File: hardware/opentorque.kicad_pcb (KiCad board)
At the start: 2 copper layers, 27 parts, among them SW1 TS-1088-AR02016, U1 RP2040, U2 W25Q128JVSIQTR, X1 X322512MSB4SI

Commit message: Arrange components
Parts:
- added C16: 100n, Capacitor_SMD:C_0603_1608Metric, F.Cu at (164.0, 103.0)
- added C17: 100n, Capacitor_SMD:C_0603_1608Metric, F.Cu at (162.5, 92.2)
- added C18: 100n, Capacitor_SMD:C_0603_1608Metric, F.Cu at (166.5, 89.0)
- added C19: RVT1J221M1010, easyeda2kicad:CAP-SMD_BD10.0-L10.3-W10.3-FD, F.Cu at (155.5, 96.0)
- added C20: 100n, Capacitor_SMD:C_0603_1608Metric, F.Cu at (184.0, 103.0)
- added C21: 100n, Capacitor_SMD:C_0603_1608Metric, F.Cu at (182.5, 92.2)
- added C22: 100n, Capacitor_SMD:C_0603_1608Metric, F.Cu at (186.5, 89.0)
- added C23: RVT1J221M1010, easyeda2kicad:CAP-SMD_BD10.0-L10.3-W10.3-FD, F.Cu at (175.5, 96.0)
- added C24: 100n, Capacitor_SMD:C_0603_1608Metric, F.Cu at (204.0, 103.0)
- added C25: 100n, Capacitor_SMD:C_0603_1608Metric, F.Cu at (202.5, 92.2)
- added C26: 100n, Capacitor_SMD:C_0603_1608Metric, F.Cu at (206.5, 89.0)
- added C27: RVT1J221M1010, easyeda2kicad:CAP-SMD_BD10.0-L10.3-W10.3-FD, F.Cu at (195.5, 96.0)
- added D1: SS14_C2837270, easyeda2kicad:SMA_L4.3-W2.6-LS5.0-RD, F.Cu at (168.5, 98.0)
- added D2: SS14_C2837270, easyeda2kicad:SMA_L4.3-W2.6-LS5.0-RD, F.Cu at (188.5, 98.0)
- added D3: SS14_C2837270, easyeda2kicad:SMA_L4.3-W2.6-LS5.0-RD, F.Cu at (208.5, 98.0)
- added GND1: TestPoint, TestPoint:TestPoint_Pad_4.0x4.0mm, F.Cu at (190.0, 72.5)
- added Q1: 30N06_C5807887, easyeda2kicad:TO-252-2_L6.6-W6.1-P4.57-LS9.9-BR-CW, F.Cu at (153.5, 82.0)
- added Q2: 30N06_C5807887, easyeda2kicad:TO-252-2_L6.6-W6.1-P4.57-LS9.9-BR-CW, F.Cu at (160.5, 84.0)
- added Q3: 30N06_C5807887, easyeda2kicad:TO-252-2_L6.6-W6.1-P4.57-LS9.9-BR-CW, F.Cu at (173.5, 82.0)
- added Q4: 30N06_C5807887, easyeda2kicad:TO-252-2_L6.6-W6.1-P4.57-LS9.9-BR-CW, F.Cu at (180.5, 84.0)
- added Q5: 30N06_C5807887, easyeda2kicad:TO-252-2_L6.6-W6.1-P4.57-LS9.9-BR-CW, F.Cu at (193.5, 82.0)
- added Q6: 30N06_C5807887, easyeda2kicad:TO-252-2_L6.6-W6.1-P4.57-LS9.9-BR-CW, F.Cu at (200.5, 84.0)
- added R10: 1m, Resistor_SMD:R_1206_3216Metric, F.Cu at (165.5, 81.5)
- added R11: 27R, Resistor_SMD:R_0603_1608Metric, F.Cu at (184.0, 92.2)
- added R12: 27R, Resistor_SMD:R_0603_1608Metric, F.Cu at (185.5, 92.2)
- added R13: 1m, Resistor_SMD:R_1206_3216Metric, F.Cu at (185.5, 81.5)
- added R14: 27R, Resistor_SMD:R_0603_1608Metric, F.Cu at (204.0, 92.2)
- added R15: 27R, Resistor_SMD:R_0603_1608Metric, F.Cu at (205.5, 92.2)
- added R16: 1m, Resistor_SMD:R_1206_3216Metric, F.Cu at (205.5, 81.5)
- added R17: 20k, Resistor_SMD:R_0603_1608Metric, F.Cu at (166.7, 124.5)
- added R18: 1k, Resistor_SMD:R_0603_1608Metric, F.Cu at (166.7, 126.0)
- added R8: 27R, Resistor_SMD:R_0603_1608Metric, F.Cu at (164.0, 92.2)
- added R9: 27R, Resistor_SMD:R_0603_1608Metric, F.Cu at (165.5, 92.2)
- added REF**: MountingHole_3.2mm_M3, MountingHole:MountingHole_3.2mm_M3, F.Cu at (153.5, 73.5)
- added REF**: MountingHole_3.2mm_M3, MountingHole:MountingHole_3.2mm_M3, F.Cu at (153.5, 126.5)
- added REF**: MountingHole_3.2mm_M3, MountingHole:MountingHole_3.2mm_M3, F.Cu at (206.5, 126.5)
- added REF**: MountingHole_3.2mm_M3, MountingHole:MountingHole_3.2mm_M3, F.Cu at (206.5, 73.5)
- added TP1: TestPoint, TestPoint:TestPoint_Pad_4.0x4.0mm, F.Cu at (160.0, 72.5)
- added TP2: TestPoint, TestPoint:TestPoint_Pad_4.0x4.0mm, F.Cu at (180.0, 72.5)
- added TP3: TestPoint, TestPoint:TestPoint_Pad_4.0x4.0mm, F.Cu at (200.0, 72.5)
- added U10: AMS1117-5.0_C347223, easyeda2kicad:SOT-223_L6.7-W3.5-P2.30-BR, F.Cu at (168.4, 109.7)
- added U11: AMS1117-3.3_C347222, easyeda2kicad:SOT-223-4_L6.5-W3.5-P2.30-LS7.0-BR, F.Cu at (168.7, 117.2)
- added U3: SLM2003ECA-DG, easyeda2kicad:SOIC-8_L4.9-W3.9-P1.27-LS6.0-BL, F.Cu at (164.0, 98.0)
- added U4: INA180A3IDBVR, easyeda2kicad:SOT-23-5_L3.0-W1.7-P0.95-LS2.8-BR, F.Cu at (166.5, 86.0)
- added U5: SLM2003ECA-DG, easyeda2kicad:SOIC-8_L4.9-W3.9-P1.27-LS6.0-BL, F.Cu at (184.0, 98.0)
- added U6: INA180A3IDBVR, easyeda2kicad:SOT-23-5_L3.0-W1.7-P0.95-LS2.8-BR, F.Cu at (186.5, 86.0)
- added U7: SLM2003ECA-DG, easyeda2kicad:SOIC-8_L4.9-W3.9-P1.27-LS6.0-BL, F.Cu at (204.0, 98.0)
- added U8: INA180A3IDBVR, easyeda2kicad:SOT-23-5_L3.0-W1.7-P0.95-LS2.8-BR, F.Cu at (206.5, 86.0)
- added U9: UMW78M12, easyeda2kicad:TO-252-2_L6.6-W6.1-P4.57-LS9.9-BR-CW, F.Cu at (158.0, 110.5)
- added VCC_12-56: TestPoint, TestPoint:TestPoint_Pad_4.0x4.0mm, F.Cu at (170.0, 72.5)
- moved R4 93.0 mm to (194.5, 124.0), turned to 90 degrees
- moved C11 91.8 mm to (200.8, 117.0)
- moved C12 91.8 mm to (200.8, 119.5)
- moved C3 91.8 mm to (196.8, 112.0)
- moved C5 91.8 mm to (196.8, 117.0)
- moved C6 91.8 mm to (196.8, 119.5)
- moved C8 91.8 mm to (200.8, 109.5)
- moved C9 91.8 mm to (200.8, 112.0)
- moved C10 91.8 mm to (200.8, 114.5)
- moved C13 91.8 mm to (204.8, 107.0)
- moved C14 91.8 mm to (204.8, 109.5)
- moved C15 91.8 mm to (204.8, 112.0)
- moved C4 91.8 mm to (196.8, 114.5)
- moved C7 91.8 mm to (200.8, 107.0)
- moved R5 89.6 mm to (196.0, 124.0), turned to 90 degrees
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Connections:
- net +1V1 renamed /rp2040/1.1V
- net +3.3V renamed /rp2040/3.3V
- net +5V renamed /rp2040/5V
- net GND renamed /rp2040/GND
- U1 pad 2: /rp2040/GPIO0 -> /phasedriver U/HIN
- U1 pad 3: /rp2040/GPIO1 -> /phasedriver U/LINN
- U1 pad 38: /rp2040/GPIO26 -> /phasedriver U/AOUT
- U1 pad 39: /rp2040/GPIO27 -> /phasedriver V/AOUT
- U1 pad 4: /rp2040/GPIO2 -> /phasedriver V/HIN
- U1 pad 40: /rp2040/GPIO28 -> /phasedriver W/AOUT
- U1 pad 41: /rp2040/GPIO29 -> /<NO NET>
- U1 pad 5: /rp2040/GPIO3 -> /phasedriver V/LINN
- U1 pad 6: /rp2040/GPIO4 -> /phasedriver W/HIN
- U1 pad 7: /rp2040/GPIO5 -> /phasedriver W/LINN
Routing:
- net /rp2040/GND: track 15.1 -> 0.00 mm
- net /rp2040/5V: track 6.66 -> 0.00 mm
- net /rp2040/DP: track 5.32 -> 0.00 mm
- net Net-(USB1-DN1): track 4.73 -> 0.00 mm
- net /rp2040/DN: track 4.70 -> 0.00 mm
- net Net-(USB1-DP1): track 4.54 -> 0.00 mm
- net Net-(USB1-CC1): track 4.32 -> 0.00 mm
- net Net-(USB1-CC2): track 3.85 -> 0.00 mm
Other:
- board outline added: 60 x 60 mm

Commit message: Add more routing
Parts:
- removed C5: 100n, Capacitor_SMD:C_0603_1608Metric
- removed R6, R7: 5k1, Resistor_SMD:R_0603_1608Metric
- removed REF** (x4): MountingHole_3.2mm_M3, MountingHole:MountingHole_3.2mm_M3
- added C28: 100n, Capacitor_SMD:C_0603_1608Metric, B.Cu at (175.8, 97.5)
- U10: value AMS1117-5.0_C347223 -> AS5600-ASOT; footprint easyeda2kicad:SOT-223_L6.7-W3.5-P2.30-BR -> easyeda2kicad:SOIC-8_L5.0-W4.0-P1.27-LS6.0-BL; moved to B.Cu
- moved C10 28.4 mm to (172.5, 117.0), turned to 180 degrees
- moved C13 26.3 mm to (178.5, 106.0), turned to 90 degrees
- moved C11 25.9 mm to (175.0, 119.5), turned to -90 degrees
- moved C6 25.8 mm to (172.5, 111.0), turned to 180 degrees
- moved C3 24.6 mm to (172.5, 115.5), turned to 180 degrees
- moved C14 24.5 mm to (182.5, 119.5), turned to -90 degrees
- moved C12 24.3 mm to (176.5, 119.5), turned to -90 degrees
- moved C9 21.2 mm to (181.0, 119.5), turned to -90 degrees
- moved C4 18.8 mm to (180.0, 106.0), turned to 90 degrees
- moved D1 16.5 mm to (152.0, 97.5)
- moved D2 16.5 mm to (172.0, 97.5)
- moved D3 16.5 mm to (192.0, 97.5)
- moved C7 15.8 mm to (186.2, 113.0)
- moved C15 15.3 mm to (196.0, 124.5), turned to 90 degrees
- moved U10 15.1 mm to (180.0, 100.0)
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- renumbered GND1 to GND, TP1 to U, TP2 to V, TP3 to W
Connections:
- C1 pad 1: /rp2040/GND -> GND
- C10 pad 1: /rp2040/3.3V -> +3V3
- C10 pad 2: /rp2040/GND -> GND
- C11 pad 1: /rp2040/3.3V -> +3V3
- C11 pad 2: /rp2040/GND -> GND
- C12 pad 2: /rp2040/GND -> GND
- C13 pad 2: /rp2040/GND -> GND
- C14 pad 2: /rp2040/GND -> GND
- C15 pad 2: /rp2040/GND -> GND
- C18 pad 1: +5V -> +3V3
- C2 pad 1: /rp2040/GND -> GND
- C22 pad 1: +5V -> +3V3
- C26 pad 1: +5V -> +3V3
- C3 pad 1: /rp2040/3.3V -> +3V3
- C3 pad 2: /rp2040/GND -> GND
- C4 pad 1: /rp2040/3.3V -> +3V3
- C4 pad 2: /rp2040/GND -> GND
- C6 pad 1: /rp2040/3.3V -> +3V3
- C6 pad 2: /rp2040/GND -> GND
- C7 pad 1: /rp2040/3.3V -> +3V3
- C7 pad 2: /rp2040/GND -> GND
- C8 pad 1: /rp2040/3.3V -> +3V3
- C8 pad 2: /rp2040/GND -> GND
- C9 pad 1: /rp2040/3.3V -> +3V3
- C9 pad 2: /rp2040/GND -> GND
- R5 pad 1: /rp2040/3.3V -> +3V3
- SW1 pad 1: /rp2040/GND -> GND
- U1 pad 1: /rp2040/3.3V -> +3V3
- U1 pad 10: /rp2040/3.3V -> +3V3
- U1 pad 13: /rp2040/GPIO10 -> /phasedriver W/HIN
- U1 pad 14: /rp2040/GPIO11 -> /phasedriver W/LINN
- U1 pad 19: /rp2040/GND -> GND
- U1 pad 2: /phasedriver U/HIN -> /rp2040/GPIO0
- U1 pad 22: /rp2040/3.3V -> +3V3
- U1 pad 26: /rp2040/3.3V -> +3V3
- U1 pad 29: /rp2040/GPIO18 -> /phasedriver V/HIN
- U1 pad 3: /phasedriver U/LINN -> /rp2040/GPIO1
- U1 pad 30: /rp2040/GPIO19 -> /phasedriver V/LINN
- U1 pad 31: /rp2040/GPIO20 -> /phasedriver U/HIN
- U1 pad 32: /rp2040/GPIO21 -> /phasedriver U/LINN
- U1 pad 33: /rp2040/3.3V -> +3V3
- U1 pad 4: /phasedriver V/HIN -> /rp2040/GPIO2
- U1 pad 42: /rp2040/3.3V -> +3V3
- U1 pad 43: /rp2040/3.3V -> +3V3
- U1 pad 44: /rp2040/3.3V -> +3V3
- U1 pad 48: /rp2040/3.3V -> +3V3
- U1 pad 49: /rp2040/3.3V -> +3V3
- U1 pad 5: /phasedriver V/LINN -> /rp2040/GPIO3
- U1 pad 57: /rp2040/GND -> GND
- U1 pad 6: /phasedriver W/HIN -> /rp2040/GPIO4
- U1 pad 7: /phasedriver W/LINN -> /rp2040/GPIO5
- U10 pad 1: GND -> +3V3
- U10 pad 2: +5V -> +3V3
- U10 pad 3: +12V -> unconnected-(U10-OUT-Pad3)
- U10 pad 4: +5V -> GND
- U11 pad 2: +3.3V -> +3V3
- U11 pad 3: +5V -> +12V
- U11 pad 4: +3.3V -> +3V3
- U2 pad 4: /rp2040/GND -> GND
- U4 pad 5: +5V -> +3V3
- U6 pad 5: +5V -> +3V3
- U8 pad 5: +5V -> +3V3
- USB1 pad 1: /rp2040/GND -> GND
- USB1 pad 10: Net-(USB1-CC2) -> unconnected-(USB1-CC2-Pad10)
- USB1 pad 11: /rp2040/5V -> unconnected-(USB1-VBUS-Pad11)
- USB1 pad 12: /rp2040/GND -> GND
- USB1 pad 13: /rp2040/GND -> GND
- USB1 pad 14: /rp2040/GND -> GND
- USB1 pad 2: /rp2040/5V -> unconnected-(USB1-VBUS-Pad2)
- USB1 pad 4: Net-(USB1-CC1) -> unconnected-(USB1-CC1-Pad4)
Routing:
- net +3V3: track 0.00 -> 160.5 mm, vias 0 -> 6
- net +12V: track 0.00 -> 88.3 mm
- net /phasedriver W/AOUT: track 0.00 -> 56.3 mm, vias 0 -> 2
- net /phasedriver V/AOUT: track 0.00 -> 38.0 mm, vias 0 -> 2
- net /phasedriver U/AOUT: track 0.00 -> 35.1 mm, vias 0 -> 2
- net Net-(Q6-S): track 0.00 -> 28.2 mm
- net Net-(Q4-S): track 0.00 -> 28.2 mm
- net Net-(Q2-S): track 0.00 -> 27.1 mm
- net /phasedriver U/HIN: track 0.00 -> 27.0 mm, vias 0 -> 2
- net Net-(Q5-S): track 0.00 -> 26.7 mm, vias 0 -> 3
- net Net-(Q3-S): track 0.00 -> 26.7 mm, vias 0 -> 3
- net Net-(Q1-S): track 0.00 -> 26.7 mm, vias 0 -> 3
- net /phasedriver U/LINN: track 0.00 -> 25.2 mm, vias 0 -> 2
- net /rp2040/1.1V: track 0.00 -> 24.4 mm, vias 0 -> 3
- net /phasedriver W/LINN: track 0.00 -> 18.6 mm, vias 0 -> 2
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- added copper zone on F.Cu, net +3V3
- added copper zone on B.Cu, net GND
- added copper zone on In1.Cu, net GND
- added copper zone on F.Cu, net VCC
- added copper zone on In2.Cu, net VCC
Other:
- copper layers 2 -> 4

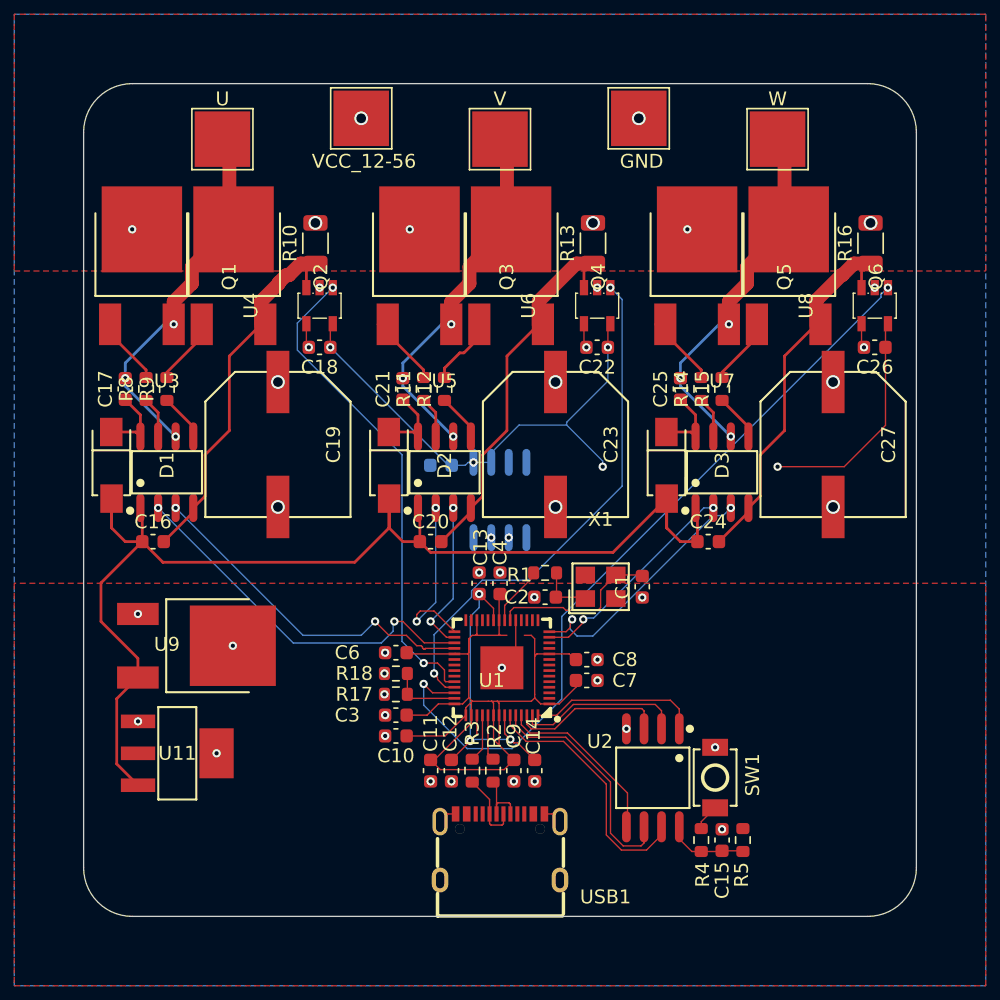
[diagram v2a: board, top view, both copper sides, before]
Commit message: Fix BOOTSEL resistors and add reset button
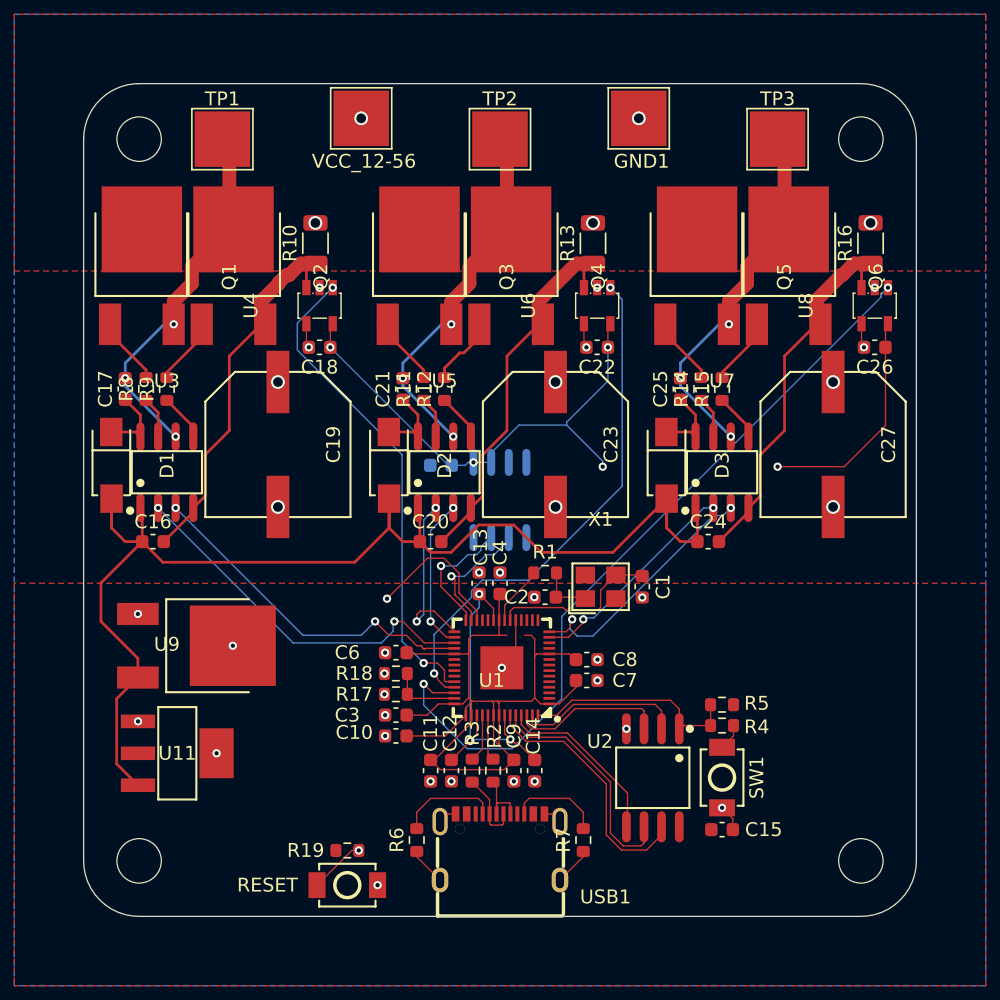
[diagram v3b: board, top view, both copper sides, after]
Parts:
- added R19: 1k, Resistor_SMD:R_0603_1608Metric, F.Cu at (169.0, 125.2)
- added R6: 5k1, Resistor_SMD:R_0603_1608Metric, F.Cu at (174.0, 124.5)
- added R7: 5k1, Resistor_SMD:R_0603_1608Metric, F.Cu at (186.0, 124.5)
- added REF**: MountingHole_3.2mm_M3, MountingHole:MountingHole_3.2mm_M3, F.Cu at (154.0, 126.0)
- added REF**: MountingHole_3.2mm_M3, MountingHole:MountingHole_3.2mm_M3, F.Cu at (206.0, 126.0)
- added REF**: MountingHole_3.2mm_M3, MountingHole:MountingHole_3.2mm_M3, F.Cu at (206.0, 74.0)
- added REF**: MountingHole_3.2mm_M3, MountingHole:MountingHole_3.2mm_M3, F.Cu at (154.0, 74.0)
- added RESET: TS-1088-AR02016, easyeda2kicad:SW-SMD_L3.9-W3.0-P4.45, F.Cu at (169.0, 127.8)
- moved R5 9.86 mm to (196.0, 114.8), turned to 180 degrees
- moved R4 8.39 mm to (196.0, 116.2), turned to 0 degrees
- moved C15 0.75 mm to (196.0, 123.8), turned to 0 degrees
- moved SW1 0.50 mm to (196.0, 120.0), turned to 90 degrees
- renumbered GND to GND1, U to TP1, V to TP2, W to TP3
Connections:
- net /<NO NET> renamed /Vsense
- C15 pad 1: Net-(U2-VCC) -> +3V3
- R4 pad 1: Net-(U2-VCC) -> /rp2040/QSPI_SS
- R5 pad 2: Net-(U2-VCC) -> /rp2040/QSPI_SS
- U1 pad 26: +3V3 -> Net-(U1-RUN)
- U1 pad 27: /rp2040/GPIO16 -> /SDA
- U1 pad 28: /rp2040/GPIO17 -> /SCL
- U10 pad 6: unconnected-(U10-SDA-Pad6) -> /SDA
- U10 pad 7: unconnected-(U10-SCL-Pad7) -> /SCL
- U2 pad 8: Net-(U2-VCC) -> +3V3
- USB1 pad 10: unconnected-(USB1-CC2-Pad10) -> Net-(USB1-CC2)
- USB1 pad 4: unconnected-(USB1-CC1-Pad4) -> Net-(USB1-CC1)
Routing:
- net Net-(U1-RUN): track 0.00 -> 33.8 mm, vias 0 -> 2
- net /SCL: track 0.00 -> 9.30 mm, vias 0 -> 1
- net /SDA: track 0.00 -> 9.15 mm, vias 0 -> 1
- net GND: track 11.9 -> 19.3 mm
- net Net-(USB1-CC1): track 0.00 -> 7.27 mm
- net Net-(USB1-CC2): track 0.00 -> 6.76 mm
- net Net-(U2-VCC): track 5.87 -> 0.00 mm
- net /rp2040/QSPI_SS: track 12.3 -> 16.2 mm
- net +12V: track 88.3 -> 89.9 mm
- net unconnected-(U10-SDA-Pad6): vias 1 -> 0
- net unconnected-(U10-SCL-Pad7): vias 1 -> 0
- net VCC: vias 9 -> 6
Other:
- outline, holes or cut-outs redrawn
